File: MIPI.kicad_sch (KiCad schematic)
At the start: 10 parts, among them IC1 ECP5-BGA256, J2 Conn_01x15, J3 USB_B_Micro

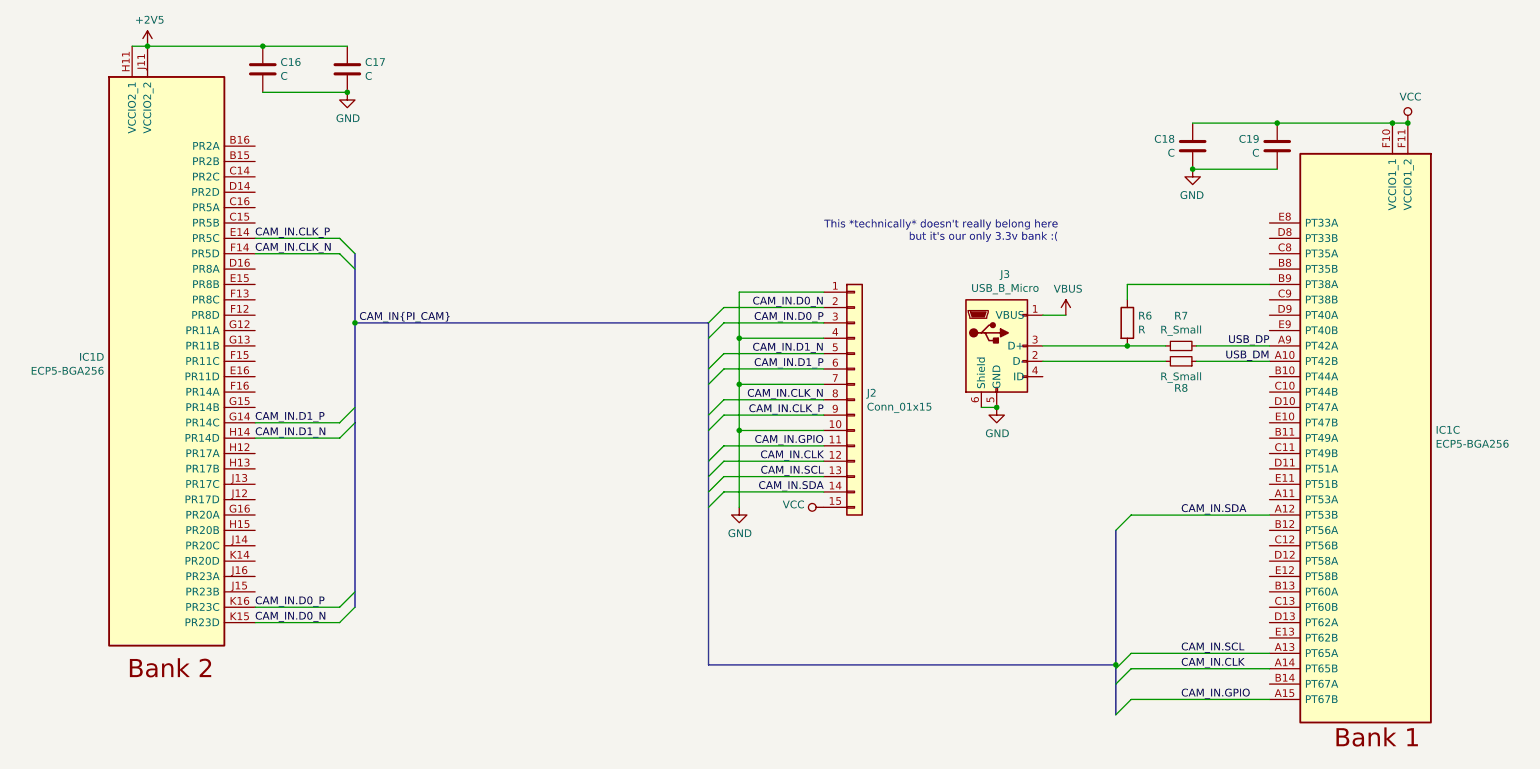
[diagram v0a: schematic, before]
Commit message: Add semi-critical resistor values
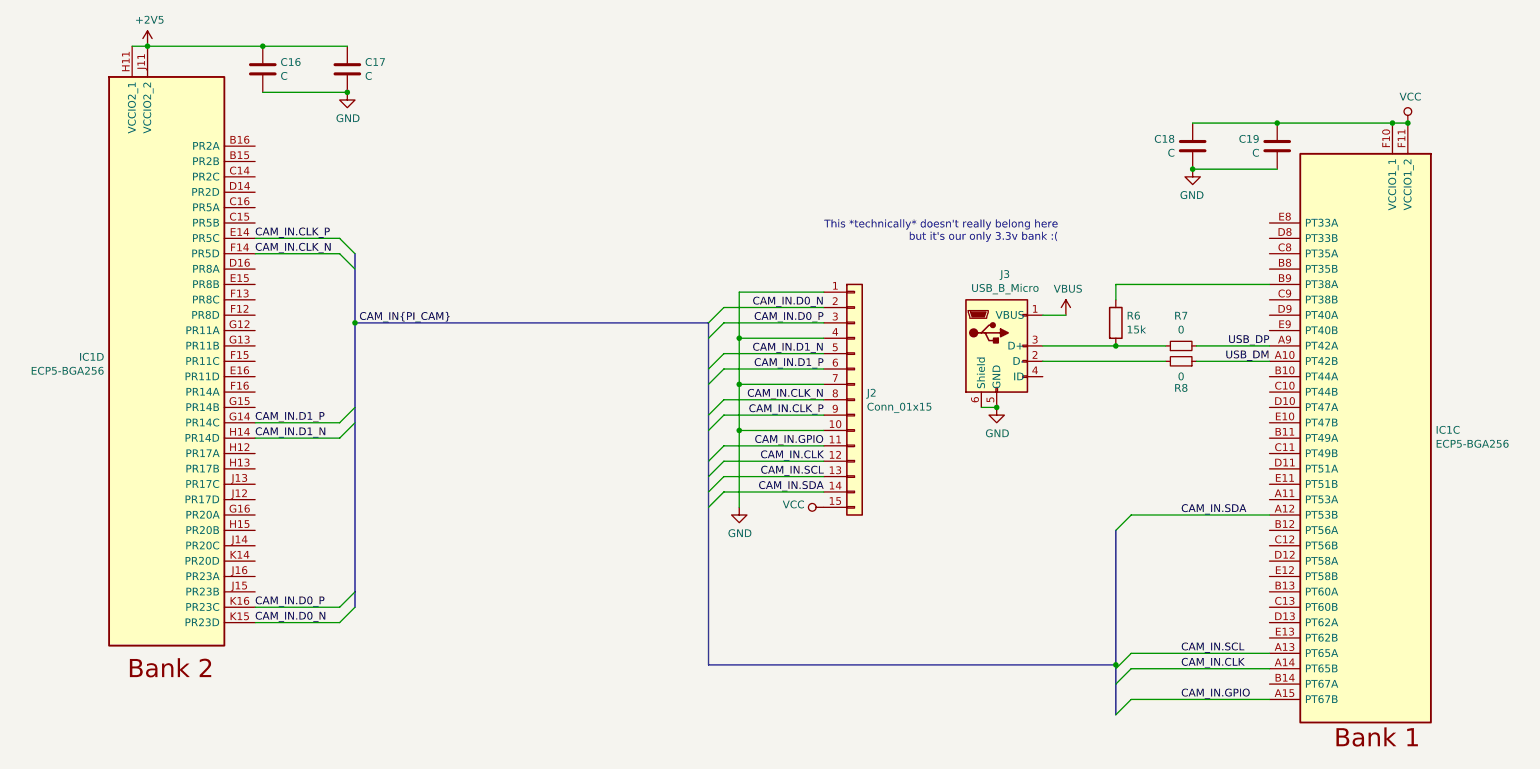
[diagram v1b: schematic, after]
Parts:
- R6: value R -> 15k
- R7, R8: value R_Small -> 0
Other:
- moved on the sheet: R6
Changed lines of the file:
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@@
-(kicad_sch (version 20200618) (host eeschema "5.99.0-unknown-7340c97~102~ubuntu20.04.1")
+(kicad_sch (version 20200618) (host eeschema "5.99.0-unknown-e9da02e~102~ubuntu20.04.1")
   (page 2 6)
   (paper "A4")
@@
   (junction (at 140.97 92.71) (diameter 0) (color 0 0 0 0))
   (junction (at 183.515 88.9) (diameter 0) (color 0 0 0 0))
-  (junction (at 205.105 78.74) (diameter 0) (color 0 0 0 0))
+  (junction (at 203.2 78.74) (diameter 0) (color 0 0 0 0))
   (junction (at 215.9 49.53) (diameter 0) (color 0 0 0 0))
   (junction (at 229.87 41.91) (diameter 0) (color 0 0 0 0))
@@
     (stroke (width 0) (type solid) (color 0 0 0 0))
   )
-  (wire (pts (xy 191.135 78.74) (xy 205.105 78.74))
+  (wire (pts (xy 191.135 78.74) (xy 203.2 78.74))
     (stroke (width 0) (type solid) (color 0 0 0 0))
   )
@@
     (stroke (width 0) (type solid) (color 0 0 0 0))
   )
-  (wire (pts (xy 205.105 68.58) (xy 228.6 68.58))
-    (stroke (width 0) (type solid) (color 0 0 0 0))
-  )
-  (wire (pts (xy 205.105 71.12) (xy 205.105 68.58))
-    (stroke (width 0) (type solid) (color 0 0 0 0))
-  )
-  (wire (pts (xy 205.105 78.74) (xy 211.455 78.74))
+  (wire (pts (xy 203.2 68.58) (xy 228.6 68.58))
+    (stroke (width 0) (type solid) (color 0 0 0 0))
+  )
+  (wire (pts (xy 203.2 71.12) (xy 203.2 68.58))
+    (stroke (width 0) (type solid) (color 0 0 0 0))
+  )
+  (wire (pts (xy 203.2 78.74) (xy 211.455 78.74))
     (stroke (width 0) (type solid) (color 0 0 0 0))
   )
@@
     (stroke (width 0) (type solid) (color 0 0 0 0))
   )
-  (bus (pts (xy 77.47 74.93) (xy 77.47 91.44))
-    (stroke (width 0) (type solid) (color 0 0 0 0))
-  )
-  (bus (pts (xy 77.47 91.44) (xy 77.47 121.92))
+  (bus (pts (xy 77.47 74.93) (xy 77.47 88.9))
+    (stroke (width 0) (type solid) (color 0 0 0 0))
+  )
+  (bus (pts (xy 77.47 88.9) (xy 77.47 119.38))
+    (stroke (width 0) (type solid) (color 0 0 0 0))
+  )
+  (bus (pts (xy 77.47 119.38) (xy 77.47 121.92))
     (stroke (width 0) (type solid) (color 0 0 0 0))
   )
@@
     (in_bom yes) (on_board yes)
     (property "Reference" "R7" (id 0) (at 213.995 73.7932 90))
-    (property "Value" "R_Small" (id 1) (at 213.995 76.0919 90))
+    (property "Value" "0" (id 1) (at 213.995 76.092 90))
     (property "Footprint" "Resistor_SMD:R_0402_1005Metric" (id 2) (at 213.995 78.74 0)
       (effects (font (size 1.27 1.27)) hide)
@@
     (in_bom yes) (on_board yes)
     (property "Reference" "R8" (id 0) (at 213.995 85.725 90))
-    (property "Value" "R_Small" (id 1) (at 213.995 83.82 90))
+    (property "Value" "0" (id 1) (at 213.995 83.82 90))
     (property "Footprint" "Resistor_SMD:R_0402_1005Metric" (id 2) (at 213.995 81.28 0)
       (effects (font (size 1.27 1.27)) hide)
@@
     )
   )
-  (symbol (lib_id "Device:R") (at 205.105 74.93 0) (unit 1)
-    (in_bom yes) (on_board yes)
-    (property "Reference" "R6" (id 0) (at 206.8831 73.7806 0)
+  (symbol (lib_id "Device:R") (at 203.2 74.93 0) (unit 1)
+    (in_bom yes) (on_board yes)
+    (property "Reference" "R6" (id 0) (at 204.9781 73.7806 0)
       (effects (font (size 1.27 1.27)) (justify left))
     )
-    (property "Value" "R" (id 1) (at 206.8831 76.0793 0)
+    (property "Value" "15k" (id 1) (at 204.978 76.079 0)
       (effects (font (size 1.27 1.27)) (justify left))
     )
-    (property "Footprint" "Resistor_SMD:R_0402_1005Metric" (id 2) (at 203.327 74.93 90)
-      (effects (font (size 1.27 1.27)) hide)
-    )
-    (property "Datasheet" "~" (id 3) (at 205.105 74.93 0)
-      (effects (font (size 1.27 1.27)) hide)
-    )
+    (property "Footprint" "Resistor_SMD:R_0402_1005Metric" (id 2) (at 201.422 74.93 90)
+      (effects (font (size 1.27 1.27)) hide)
+    )
+    (property "Datasheet" "~" (id 3) (at 203.2 74.93 0)
+      (effects (font (size 1.27 1.27)) hide)
+    )

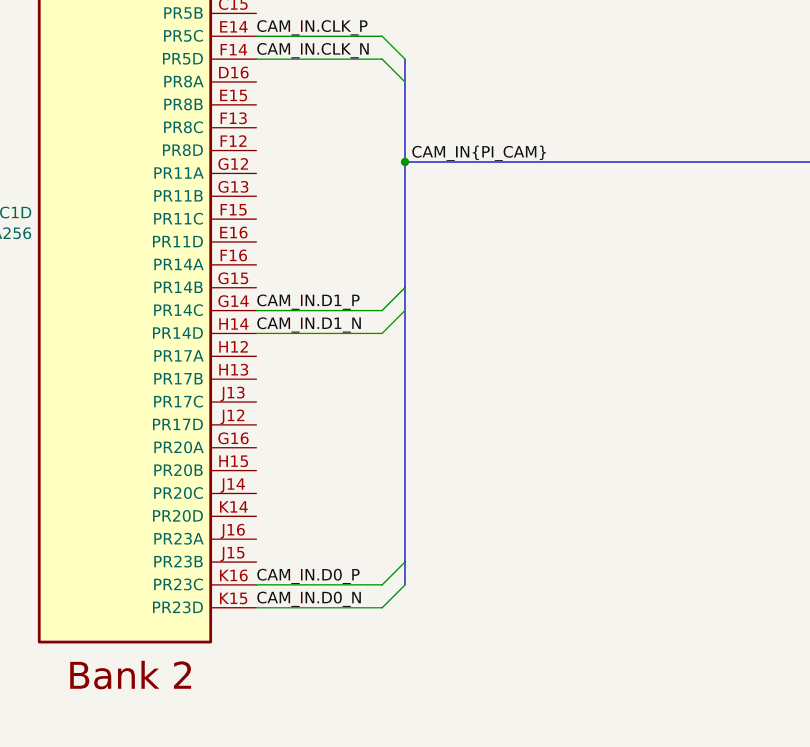
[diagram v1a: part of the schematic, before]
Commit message: Add more pullup resistors
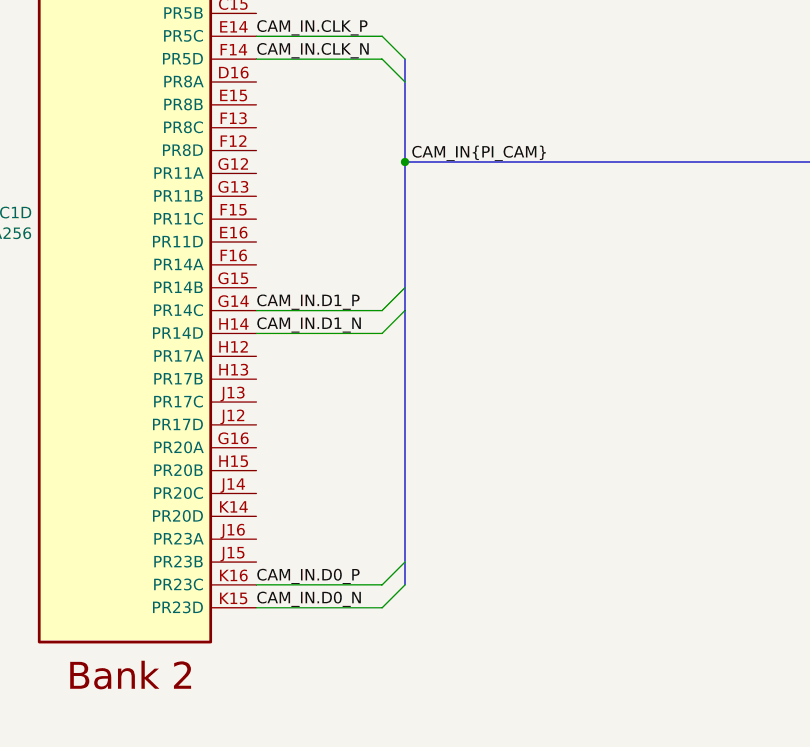
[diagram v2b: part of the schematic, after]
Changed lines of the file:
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@@
-(kicad_sch (version 20200618) (host eeschema "5.99.0-unknown-e9da02e~102~ubuntu20.04.1")
-  (page 2 6)
+(kicad_sch (version 20200714) (host eeschema "5.99.0-unknown-9f20c61~102~ubuntu20.04.1")
+  (page 1 6)
   (paper "A4")
   (bus_alias "PI_CAM" (members "D0_P" "D0_N" "D1_P" "D1_N" "CLK_P" "CLK_N" "GPIO" "CLK" "SCL" "SDA"))
@@
     (stroke (width 0) (type solid) (color 0 0 0 0))
   )
-  (bus (pts (xy 77.47 74.93) (xy 77.47 88.9))
-    (stroke (width 0) (type solid) (color 0 0 0 0))
-  )
-  (bus (pts (xy 77.47 88.9) (xy 77.47 119.38))
-    (stroke (width 0) (type solid) (color 0 0 0 0))
-  )
-  (bus (pts (xy 77.47 119.38) (xy 77.47 121.92))
-    (stroke (width 0) (type solid) (color 0 0 0 0))
-  )
+  (bus (pts (xy 77.47 74.93) (xy 77.47 91.44))
+    (stroke (width 0) (type solid) (color 0 0 0 0))
+  )
+  (bus (pts (xy 77.47 91.44) (xy 77.47 121.92))
+    (stroke (width 0) (type solid) (color 0 0 0 0))
+  )

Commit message: Change oscillator to SI5315, change RGB LED
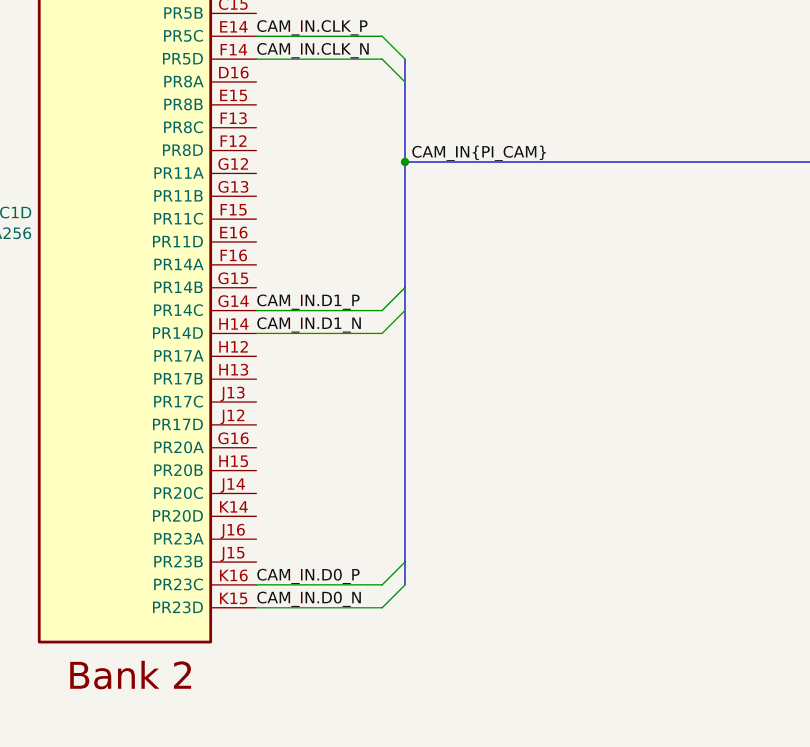
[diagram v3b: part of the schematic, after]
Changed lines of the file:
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@@
-(kicad_sch (version 20200714) (host eeschema "5.99.0-unknown-9f20c61~102~ubuntu20.04.1")
-  (page 1 6)
+(kicad_sch (version 20200714) (host eeschema "5.99.0-unknown-20c1492~102~ubuntu20.04.1")
+  (page 2 6)
   (paper "A4")
   (bus_alias "PI_CAM" (members "D0_P" "D0_N" "D1_P" "D1_N" "CLK_P" "CLK_N" "GPIO" "CLK" "SCL" "SDA"))
@@
     (stroke (width 0) (type solid) (color 0 0 0 0))
   )
-  (bus (pts (xy 77.47 74.93) (xy 77.47 91.44))
-    (stroke (width 0) (type solid) (color 0 0 0 0))
-  )
-  (bus (pts (xy 77.47 91.44) (xy 77.47 121.92))
-    (stroke (width 0) (type solid) (color 0 0 0 0))
-  )
+  (bus (pts (xy 77.47 74.93) (xy 77.47 88.9))
+    (stroke (width 0) (type solid) (color 0 0 0 0))
+  )
+  (bus (pts (xy 77.47 88.9) (xy 77.47 119.38))
+    (stroke (width 0) (type solid) (color 0 0 0 0))
+  )
+  (bus (pts (xy 77.47 119.38) (xy 77.47 121.92))
+    (stroke (width 0) (type solid) (color 0 0 0 0))
+  )
